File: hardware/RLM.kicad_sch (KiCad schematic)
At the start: 1 part, among them U1 ESP32-DEVKIT-V1

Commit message: feat: add nRF module
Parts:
- added U2: NRF24L01+, RF_Module:nRF24L01_Breakout, symbol RF:NRF24L01_Breakout
- U1: value ESP32-DEVKIT-V1 -> ESP32; footprint ESP32-DEVKIT-V1:MODULE_ESP32_DEVKIT_V1 -> GRC:MODULE_ESP32_DEVKIT_V1
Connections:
- net 3V3: now reaches U1.1 (3V3)
- net 3V3: now also U2.2 (VCC)
- net NRF_MISO: now reaches U1.10 (D19)
- net NRF_MISO: now also U2.7 (MISO)
- net GND: now reaches U1.2 (GND), U1.29 (GND)
- net GND: now also U2.1 (GND)
- net NRF_MOSI: now reaches U1.23 (D25)
- net NRF_MOSI: now also U2.6 (MOSI)
- net NRF_CE: now reaches U1.5 (D4)
- net NRF_CE: now also U2.3 (CE)
- net NRF_CSN: now reaches U1.8 (D5)
- net NRF_CSN: now also U2.4 (~{CSN})
- net NRF_SCK: now reaches U1.9 (D18)
- net NRF_SCK: now also U2.5 (SCK)
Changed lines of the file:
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@@
 (kicad_sch (version 20230121) (generator eeschema)
   (paper "A4")
+  (global_label "NRF_MISO" (shape input) (at 125.73 128.27 180) (fields_autoplaced)
+    (effects (font (size 1.27 1.27)) (justify right))
+    (property "Intersheetrefs" "${INTERSHEET_REFS}" (at 113.4919 128.27 0)
+      (effects (font (size 1.27 1.27)) (justify right) hide)
+    )
+  )
+  (global_label "GND" (shape input) (at 201.93 119.38 270) (fields_autoplaced)
+    (effects (font (size 1.27 1.27)) (justify right))
+    (property "Intersheetrefs" "${INTERSHEET_REFS}" (at 201.93 126.2357 90)
+      (effects (font (size 1.27 1.27)) (justify right) hide)
+    )
+  )
+  (global_label "NRF_MISO" (shape input) (at 189.23 99.06 180) (fields_autoplaced)
+    (effects (font (size 1.27 1.27)) (justify right))
+    (property "Intersheetrefs" "${INTERSHEET_REFS}" (at 176.9919 99.06 0)
+      (effects (font (size 1.27 1.27)) (justify right) hide)
+    )
+  )
+  (global_label "NRF_CSN" (shape input) (at 125.73 113.03 180) (fields_autoplaced)
+    (effects (font (size 1.27 1.27)) (justify right))
+    (property "Intersheetrefs" "${INTERSHEET_REFS}" (at 114.2781 113.03 0)
+      (effects (font (size 1.27 1.27)) (justify right) hide)
+    )
+  )
+  (global_label "NRF_MOSI" (shape input) (at 156.21 113.03 0) (fields_autoplaced)
+    (effects (font (size 1.27 1.27)) (justify left))
+    (property "Intersheetrefs" "${INTERSHEET_REFS}" (at 168.4481 113.03 0)
+      (effects (font (size 1.27 1.27)) (justify left) hide)
+    )
+  )
+  (global_label "3V3" (shape input) (at 201.93 88.9 90) (fields_autoplaced)
+    (effects (font (size 1.27 1.27)) (justify left))
+    (property "Intersheetrefs" "${INTERSHEET_REFS}" (at 201.93 82.4072 90)
+      (effects (font (size 1.27 1.27)) (justify left) hide)
+    )
+  )
+  (global_label "GND" (shape input) (at 156.21 135.89 0) (fields_autoplaced)
+    (effects (font (size 1.27 1.27)) (justify left))
+    (property "Intersheetrefs" "${INTERSHEET_REFS}" (at 163.0657 135.89 0)
+      (effects (font (size 1.27 1.27)) (justify left) hide)
+    )
+  )
+  (global_label "NRF_CE" (shape input) (at 189.23 109.22 180) (fields_autoplaced)
+    (effects (font (size 1.27 1.27)) (justify right))
+    (property "Intersheetrefs" "${INTERSHEET_REFS}" (at 179.1691 109.22 0)
+      (effects (font (size 1.27 1.27)) (justify right) hide)
+    )
+  )
+  (global_label "NRF_SCK" (shape input) (at 189.23 101.6 180) (fields_autoplaced)
+    (effects (font (size 1.27 1.27)) (justify right))
+    (property "Intersheetrefs" "${INTERSHEET_REFS}" (at 177.8386 101.6 0)
+      (effects (font (size 1.27 1.27)) (justify right) hide)
+    )
+  )
+  (global_label "NRF_CSN" (shape input) (at 189.23 104.14 180) (fields_autoplaced)
+    (effects (font (size 1.27 1.27)) (justify right))
+    (property "Intersheetrefs" "${INTERSHEET_REFS}" (at 177.7781 104.14 0)
+      (effects (font (size 1.27 1.27)) (justify right) hide)
+    )
+  )
+  (global_label "NRF_SCK" (shape input) (at 125.73 125.73 180) (fields_autoplaced)
+    (effects (font (size 1.27 1.27)) (justify right))
+    (property "Intersheetrefs" "${INTERSHEET_REFS}" (at 114.3386 125.73 0)
+      (effects (font (size 1.27 1.27)) (justify right) hide)
+    )
+  )
+  (global_label "NRF_MOSI" (shape input) (at 189.23 96.52 180) (fields_autoplaced)
+    (effects (font (size 1.27 1.27)) (justify right))
+    (property "Intersheetrefs" "${INTERSHEET_REFS}" (at 176.9919 96.52 0)
+      (effects (font (size 1.27 1.27)) (justify right) hide)
+    )
+  )
+  (global_label "3V3" (shape input) (at 156.21 85.09 0) (fields_autoplaced)
+    (effects (font (size 1.27 1.27)) (justify left))
+    (property "Intersheetrefs" "${INTERSHEET_REFS}" (at 162.7028 85.09 0)
+      (effects (font (size 1.27 1.27)) (justify left) hide)
+    )
+  )
+  (global_label "NRF_CE" (shape input) (at 125.73 110.49 180) (fields_autoplaced)
+    (effects (font (size 1.27 1.27)) (justify right))
+    (property "Intersheetrefs" "${INTERSHEET_REFS}" (at 115.6691 110.49 0)
+      (effects (font (size 1.27 1.27)) (justify right) hide)
+    )
+  )
+  (symbol (lib_id "RF:NRF24L01_Breakout") (at 201.93 104.14 0) (unit 1)
+    (in_bom yes) (on_board yes) (dnp no) (fields_autoplaced)
+    (property "Reference" "U2" (at 212.09 102.87 0)
+      (effects (font (size 1.27 1.27)) (justify left))
+    )
+    (property "Value" "NRF24L01+" (at 212.09 105.41 0)
+      (effects (font (size 1.27 1.27)) (justify left))
+    )
+    (property "Footprint" "RF_Module:nRF24L01_Breakout" (at 205.74 88.9 0)
+      (effects (font (size 1.27 1.27) italic) (justify left) hide)
+    )
+    (property "Datasheet" "http://www.nordicsemi.com/eng/content/download/2730/34105/file/nRF24L01_Product_Specification_v2_0.pdf" (at 201.93 106.68 0)
+      (effects (font (size 1.27 1.27)) hide)
+    )
+    (pin "1")
+    (pin "2")
+    (pin "3")
+    (pin "4")
+    (pin "5")
+    (pin "6")
+    (pin "7")
+    (pin "8")
+    (instances
+      (project "RLM"
+        (path "/3fe8a1ac-6190-4220-82eb-f4588302947e"
+          (reference "U2") (unit 1)
+        )
+      )
+    )
+  )
   (symbol (lib_id "GRC_ESP32-DEVKIT-V1:ESP32-DEVKIT-V1") (at 140.97 110.49 0) (unit 1)
     (in_bom yes) (on_board yes) (dnp no) (fields_autoplaced)
@@
       (effects (font (size 1.27 1.27)))
     )
-    (property "Value" "ESP32-DEVKIT-V1" (at 140.97 80.01 0)
+    (property "Value" "ESP32" (at 140.97 80.01 0)
       (effects (font (size 1.27 1.27)))
     )
-    (property "Footprint" "ESP32-DEVKIT-V1:MODULE_ESP32_DEVKIT_V1" (at 140.97 110.49 0)
+    (property "Footprint" "GRC:MODULE_ESP32_DEVKIT_V1" (at 140.97 110.49 0)
       (effects (font (size 1.27 1.27)) (justify bottom) hide)
     )

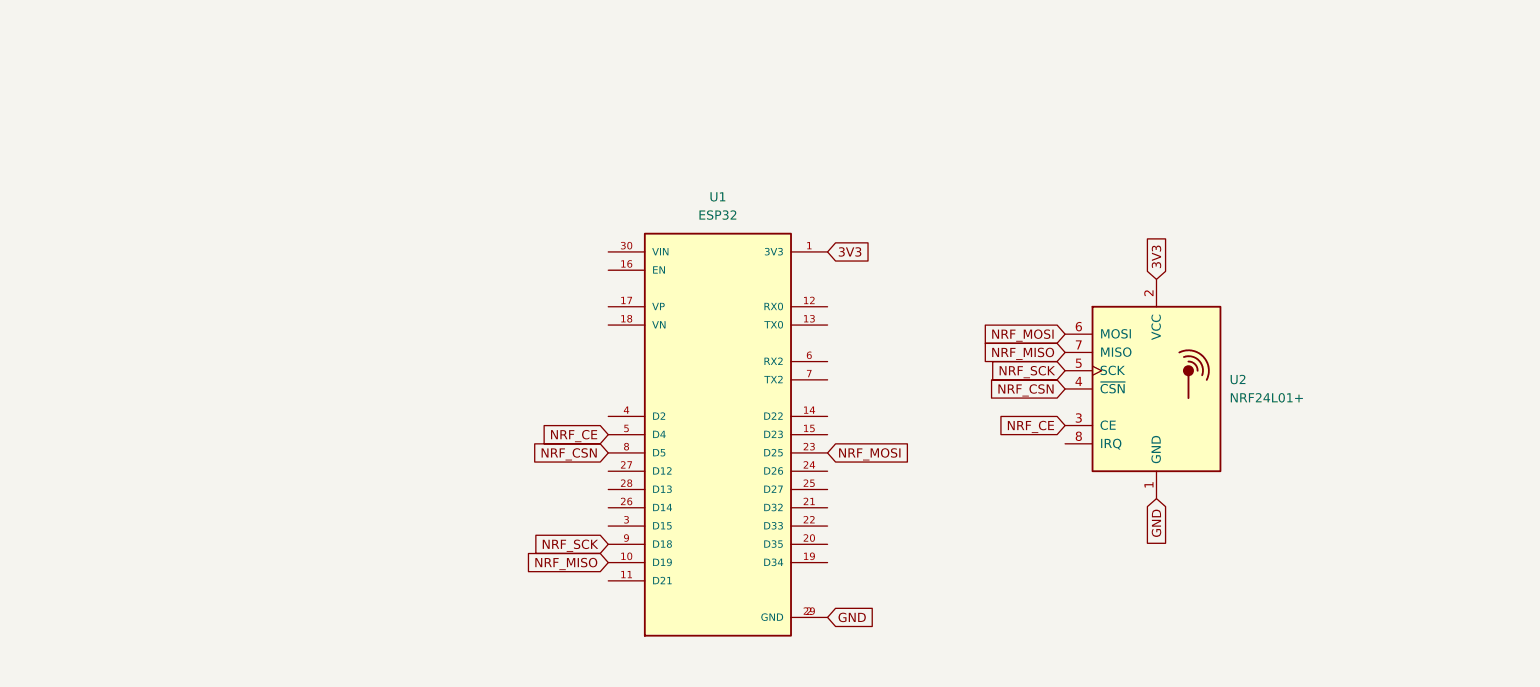
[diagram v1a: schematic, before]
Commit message: feat: add MPU-6050
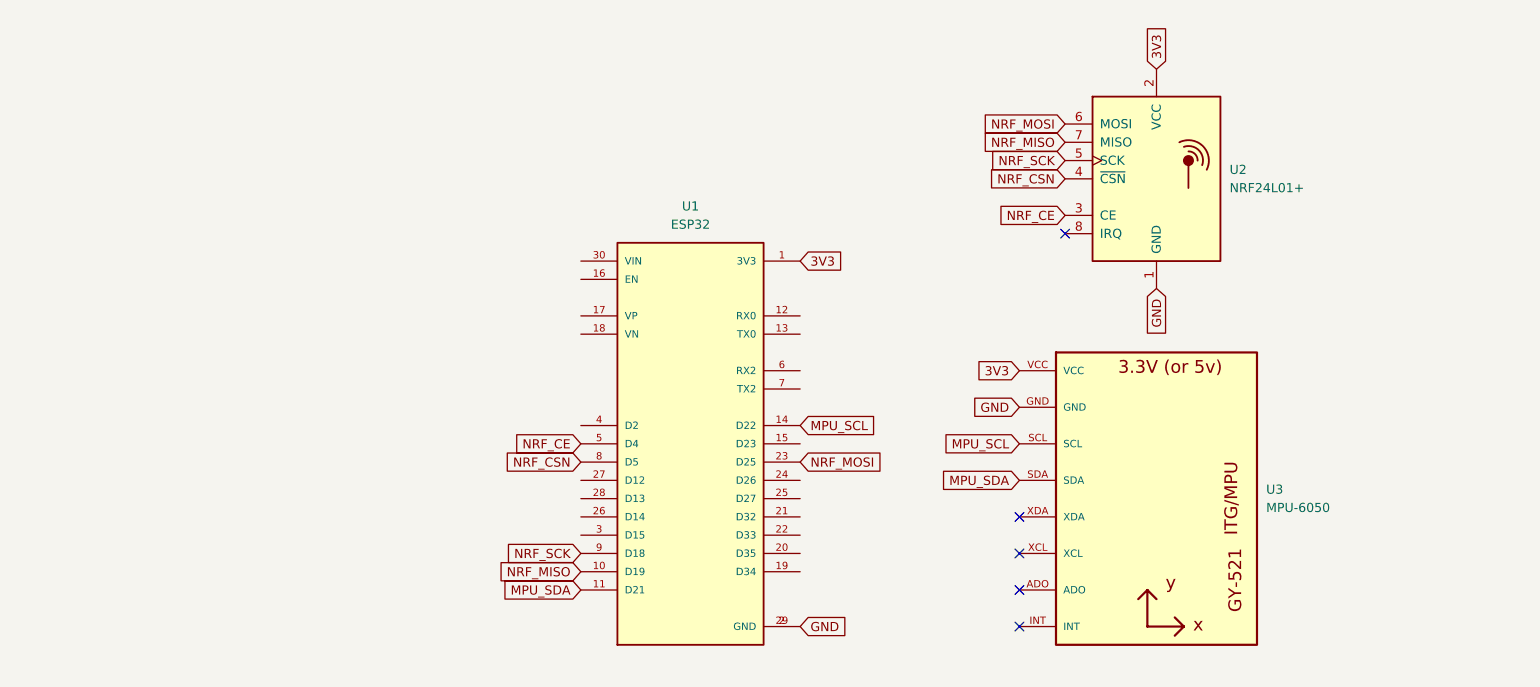
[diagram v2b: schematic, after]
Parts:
- added U3: MPU-6050, GRC:GY-521, symbol GRC_GY-521:GY-521
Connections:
- net 3V3: now also U3.VCC
- net GND: now also U3.GND
- net MPU_SDA: now reaches U1.11 (D21)
- net MPU_SDA: now also U3.SDA
- net MPU_SCL: now reaches U1.14 (D22)
- net MPU_SCL: now also U3.SCL
- no-connect marks 0 -> 5
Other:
- moved on the sheet: U1, U2

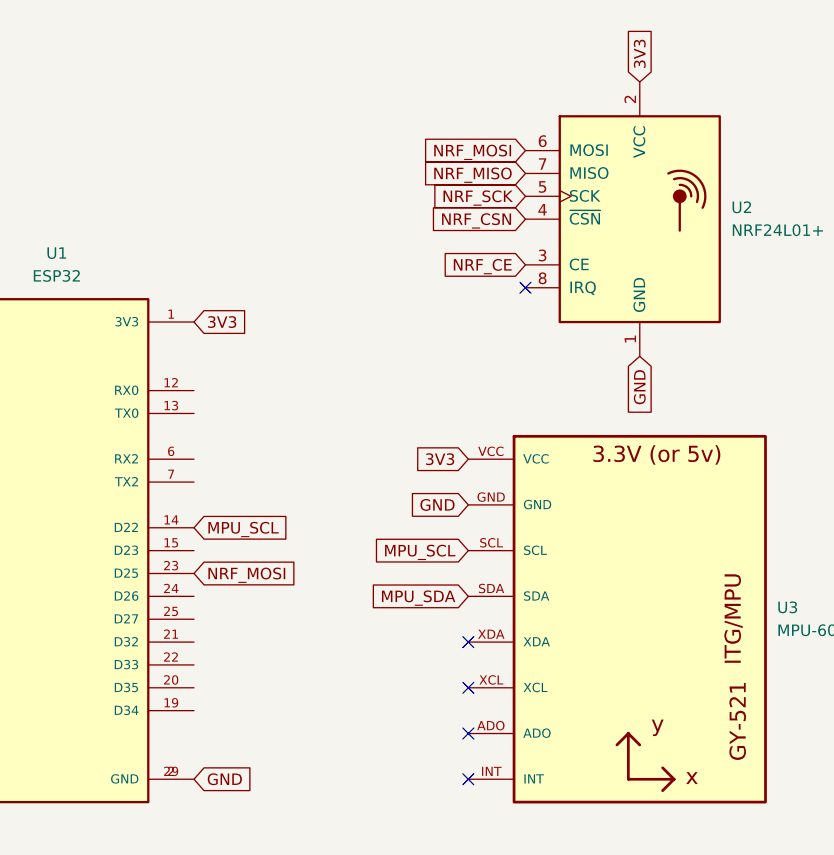
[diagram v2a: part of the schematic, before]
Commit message: feat: add MPU-6050
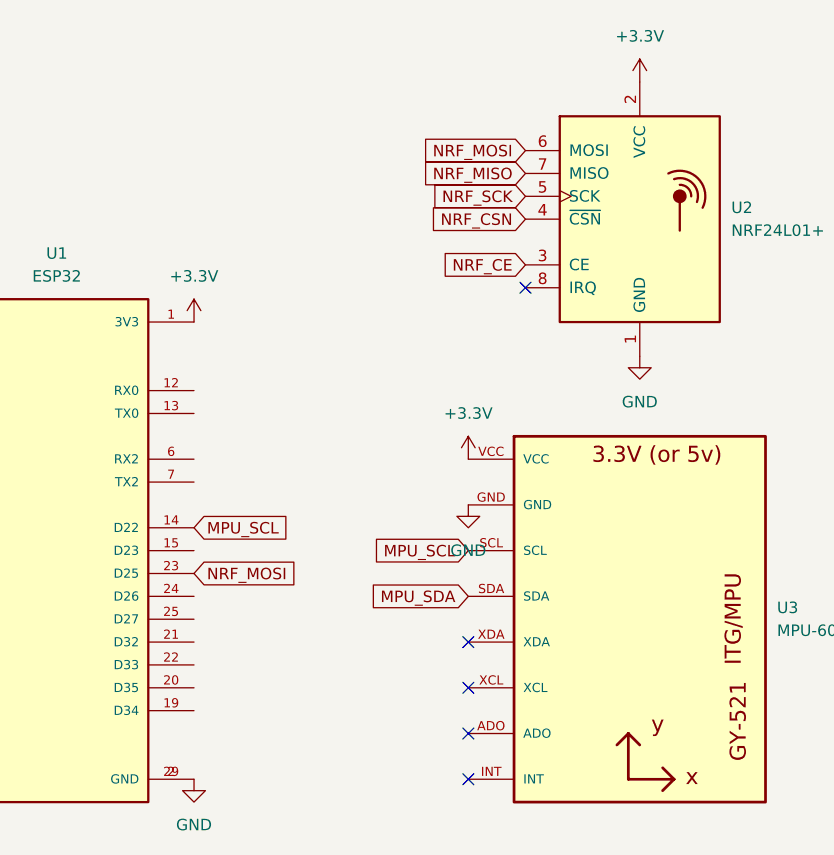
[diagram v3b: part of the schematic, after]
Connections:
- net 3V3 renamed +3.3V
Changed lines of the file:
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@@
-    )
-  )
-  (global_label "GND" (shape input) (at 201.93 90.17 270) (fields_autoplaced)
-    (effects (font (size 1.27 1.27)) (justify right))
-    (property "Intersheetrefs" "${INTERSHEET_REFS}" (at 201.93 97.0257 90)
-      (effects (font (size 1.27 1.27)) (justify right) hide)
     )
   )
@@
     (effects (font (size 1.27 1.27)) (justify right))
     (property "Intersheetrefs" "${INTERSHEET_REFS}" (at 176.9919 69.85 0)
-      (effects (font (size 1.27 1.27)) (justify right) hide)
-    )
-  )
-  (global_label "GND" (shape input) (at 182.88 106.68 180) (fields_autoplaced)
-    (effects (font (size 1.27 1.27)) (justify right))
-    (property "Intersheetrefs" "${INTERSHEET_REFS}" (at 176.0243 106.68 0)
       (effects (font (size 1.27 1.27)) (justify right) hide)
     )
@@
     )
   )
-  (global_label "3V3" (shape input) (at 201.93 59.69 90) (fields_autoplaced)
-    (effects (font (size 1.27 1.27)) (justify left))
-    (property "Intersheetrefs" "${INTERSHEET_REFS}" (at 201.93 53.1972 90)
-      (effects (font (size 1.27 1.27)) (justify left) hide)
-    )
-  )
-  (global_label "GND" (shape input) (at 152.4 137.16 0) (fields_autoplaced)
-    (effects (font (size 1.27 1.27)) (justify left))
-    (property "Intersheetrefs" "${INTERSHEET_REFS}" (at 159.2557 137.16 0)
-      (effects (font (size 1.27 1.27)) (justify left) hide)
-    )
-  )
   (global_label "MPU_SCL" (shape input) (at 152.4 109.22 0) (fields_autoplaced)
     (effects (font (size 1.27 1.27)) (justify left))
@@
     )
   )
-  (global_label "3V3" (shape input) (at 182.88 101.6 180) (fields_autoplaced)
-    (effects (font (size 1.27 1.27)) (justify right))
-    (property "Intersheetrefs" "${INTERSHEET_REFS}" (at 176.3872 101.6 0)
-      (effects (font (size 1.27 1.27)) (justify right) hide)
-    )
-  )
   (global_label "NRF_CSN" (shape input) (at 189.23 74.93 180) (fields_autoplaced)
     (effects (font (size 1.27 1.27)) (justify right))
@@
     )
   )
-  (global_label "3V3" (shape input) (at 152.4 86.36 0) (fields_autoplaced)
-    (effects (font (size 1.27 1.27)) (justify left))
-    (property "Intersheetrefs" "${INTERSHEET_REFS}" (at 158.8928 86.36 0)
-      (effects (font (size 1.27 1.27)) (justify left) hide)
-    )
-  )
   (global_label "NRF_CE" (shape input) (at 121.92 111.76 180) (fields_autoplaced)
     (effects (font (size 1.27 1.27)) (justify right))
     (property "Intersheetrefs" "${INTERSHEET_REFS}" (at 111.8591 111.76 0)
       (effects (font (size 1.27 1.27)) (justify right) hide)
+    )
+  )
+  (symbol (lib_id "power:+3.3V") (at 152.4 86.36 0) (unit 1)
+    (in_bom yes) (on_board yes) (dnp no) (fields_autoplaced)
+    (property "Reference" "#PWR03" (at 152.4 90.17 0)
+      (effects (font (size 1.27 1.27)) hide)
+    )
+    (property "Value" "+3.3V" (at 152.4 81.28 0)
+      (effects (font (size 1.27 1.27)))
+    )
+    (property "Footprint" "" (at 152.4 86.36 0)
+      (effects (font (size 1.27 1.27)) hide)
+    )
+    (property "Datasheet" "" (at 152.4 86.36 0)
+      (effects (font (size 1.27 1.27)) hide)
+    )
+    (pin "1")
+    (instances
+      (project "RLM"
+        (path "/3fe8a1ac-6190-4220-82eb-f4588302947e"
+          (reference "#PWR03") (unit 1)
+        )
+      )
     )
   )
@@
         (path "/3fe8a1ac-6190-4220-82eb-f4588302947e"
           (reference "U3") (unit 1)
+        )
+      )
+    )
+  )
+  (symbol (lib_id "power:GND") (at 201.93 90.17 0) (unit 1)
+    (in_bom yes) (on_board yes) (dnp no) (fields_autoplaced)
+    (property "Reference" "#PWR02" (at 201.93 96.52 0)
+      (effects (font (size 1.27 1.27)) hide)
+    )
+    (property "Value" "GND" (at 201.93 95.25 0)
+      (effects (font (size 1.27 1.27)))
+    )
+    (property "Footprint" "" (at 201.93 90.17 0)
+      (effects (font (size 1.27 1.27)) hide)
+    )
+    (property "Datasheet" "" (at 201.93 90.17 0)
+      (effects (font (size 1.27 1.27)) hide)
+    )
+    (pin "1")
+    (instances
+      (project "RLM"
+        (path "/3fe8a1ac-6190-4220-82eb-f4588302947e"
+          (reference "#PWR02") (unit 1)
+        )
+      )
+    )
+  )
+  (symbol (lib_id "power:GND") (at 182.88 106.68 0) (unit 1)
+    (in_bom yes) (on_board yes) (dnp no) (fields_autoplaced)
+    (property "Reference" "#PWR06" (at 182.88 113.03 0)
+      (effects (font (size 1.27 1.27)) hide)
+    )
+    (property "Value" "GND" (at 182.88 111.76 0)
+      (effects (font (size 1.27 1.27)))
+    )
+    (property "Footprint" "" (at 182.88 106.68 0)
+      (effects (font (size 1.27 1.27)) hide)
+    )
+    (property "Datasheet" "" (at 182.88 106.68 0)
+      (effects (font (size 1.27 1.27)) hide)
+    )
+    (pin "1")
+    (instances
+      (project "RLM"
+        (path "/3fe8a1ac-6190-4220-82eb-f4588302947e"
+          (reference "#PWR06") (unit 1)
+        )
+      )
+    )
+  )
+  (symbol (lib_id "power:GND") (at 152.4 137.16 0) (unit 1)
+    (in_bom yes) (on_board yes) (dnp no) (fields_autoplaced)
+    (property "Reference" "#PWR05" (at 152.4 143.51 0)
+      (effects (font (size 1.27 1.27)) hide)
+    )
+    (property "Value" "GND" (at 152.4 142.24 0)
+      (effects (font (size 1.27 1.27)))
+    )
+    (property "Footprint" "" (at 152.4 137.16 0)
+      (effects (font (size 1.27 1.27)) hide)
+    )
+    (property "Datasheet" "" (at 152.4 137.16 0)
+      (effects (font (size 1.27 1.27)) hide)
+    )
+    (pin "1")
+    (instances
+      (project "RLM"
+        (path "/3fe8a1ac-6190-4220-82eb-f4588302947e"
+          (reference "#PWR05") (unit 1)
+        )
+      )
+    )
+  )
+  (symbol (lib_id "power:+3.3V") (at 182.88 101.6 0) (unit 1)
+    (in_bom yes) (on_board yes) (dnp no) (fields_autoplaced)
+    (property "Reference" "#PWR04" (at 182.88 105.41 0)
+      (effects (font (size 1.27 1.27)) hide)
+    )
+    (property "Value" "+3.3V" (at 182.88 96.52 0)
+      (effects (font (size 1.27 1.27)))
+    )
+    (property "Footprint" "" (at 182.88 101.6 0)
+      (effects (font (size 1.27 1.27)) hide)
+    )
+    (property "Datasheet" "" (at 182.88 101.6 0)
+      (effects (font (size 1.27 1.27)) hide)
+    )
+    (pin "1")
+    (instances
+      (project "RLM"
+        (path "/3fe8a1ac-6190-4220-82eb-f4588302947e"
+          (reference "#PWR04") (unit 1)
         )
       )
@@
         )
       )
+    )
+  )
+  (symbol (lib_id "power:+3.3V") (at 201.93 59.69 0) (unit 1)
+    (in_bom yes) (on_board yes) (dnp no) (fields_autoplaced)
+    (property "Reference" "#PWR01" (at 201.93 63.5 0)
+      (effects (font (size 1.27 1.27)) hide)
+    )
+    (property "Value" "+3.3V" (at 201.93 54.61 0)
+      (effects (font (size 1.27 1.27)))
+    )
+    (property "Footprint" "" (at 201.93 59.69 0)
+      (effects (font (size 1.27 1.27)) hide)
+    )
+    (property "Datasheet" "" (at 201.93 59.69 0)
+      (effects (font (size 1.27 1.27)) hide)
+    )
+    (pin "1")
+    (instances
+      (project "RLM"
+        (path "/3fe8a1ac-6190-4220-82eb-f4588302947e"
+          (reference "#PWR01") (unit 1)
+        )
+      )
